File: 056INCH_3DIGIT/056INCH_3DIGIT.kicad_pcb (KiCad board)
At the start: 2 copper layers, 43.8 x 21 mm, 2 parts, among them U1 BA56-12SRWA

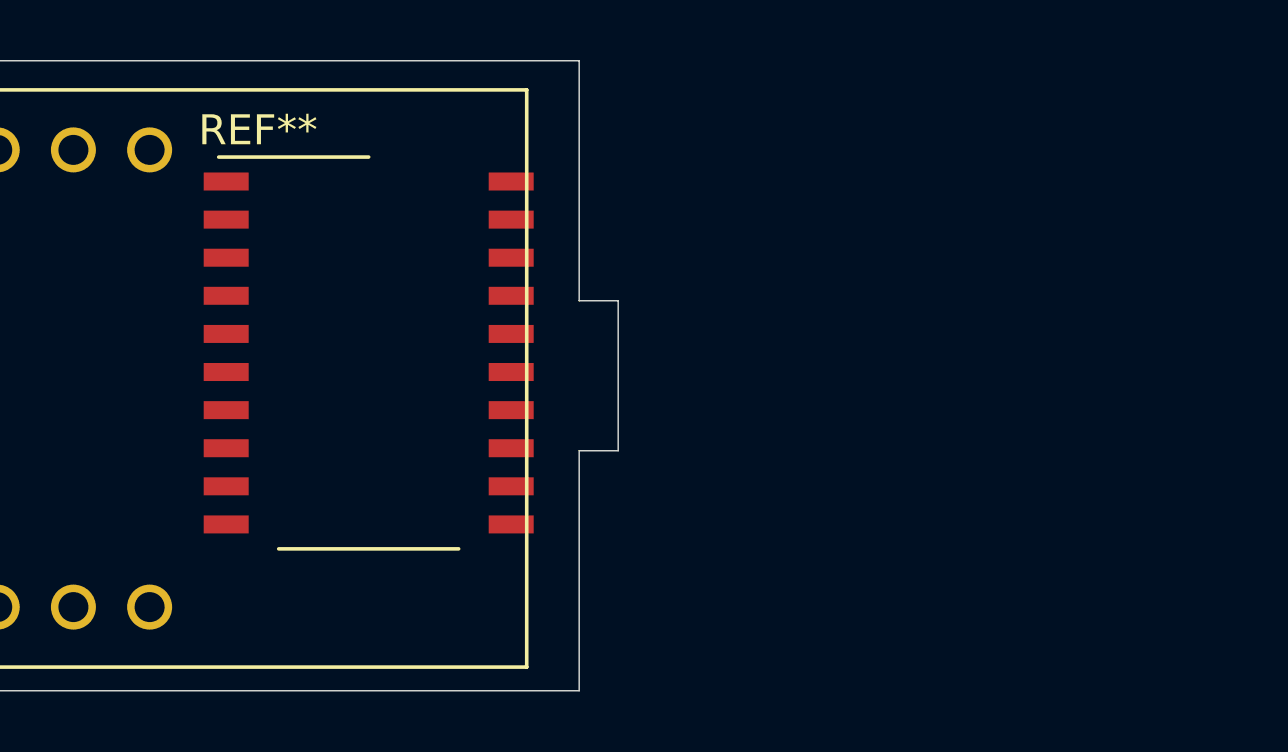
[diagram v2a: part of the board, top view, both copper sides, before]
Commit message: TM1637 symbol finished
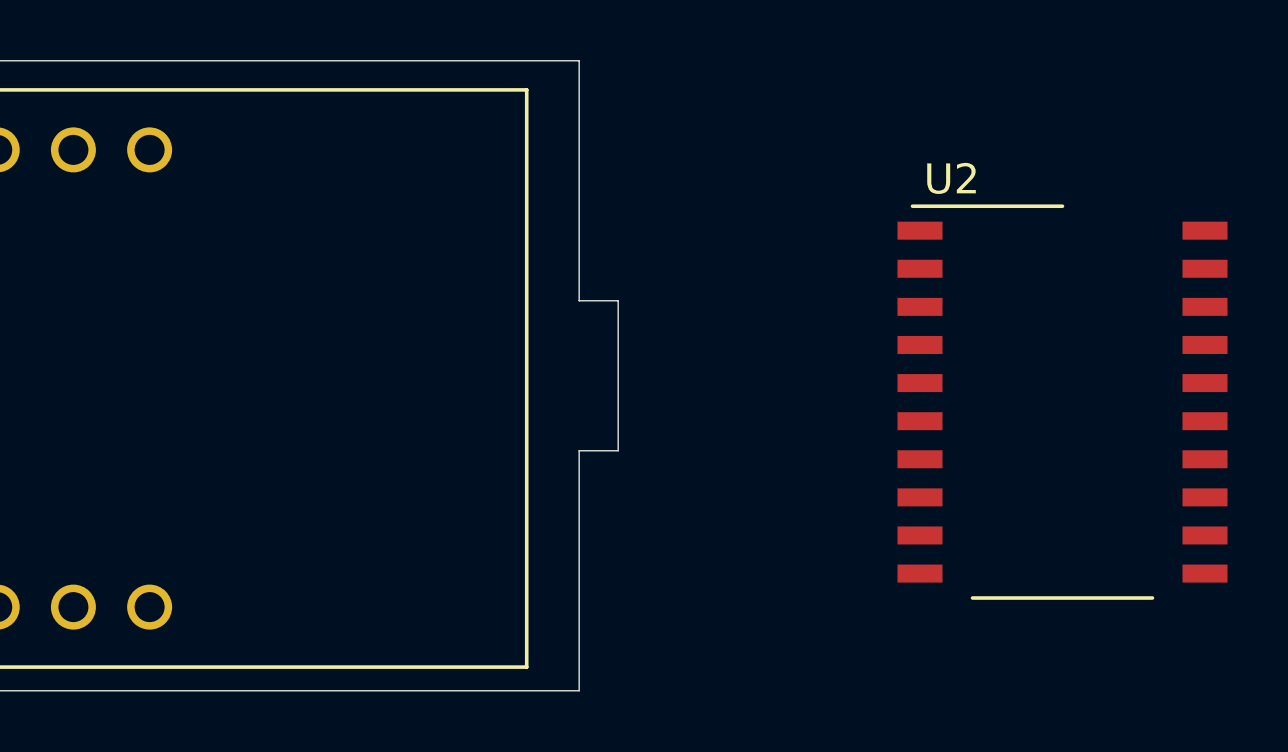
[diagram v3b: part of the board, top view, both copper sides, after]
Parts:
- removed REF**: SO-20_12.8x7.5mm_P1.27mm, Package_SO:SO-20_12.8x7.5mm_P1.27mm
- added U2: TM1637, Package_SO:SO-20_12.8x7.5mm_P1.27mm, F.Cu at (158.6, 111.4)
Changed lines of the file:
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@@
     (zones 0)
     (modules 2)
-    (nets 13)
+    (nets 30)
   )
   (page A4)
@@
   (net 11 "Net-(U1-Pad2)")
   (net 12 "Net-(U1-Pad1)")
+  (net 13 "Net-(U2-Pad18)")
+  (net 14 "Net-(U2-Pad17)")
+  (net 15 "Net-(U2-Pad16)")
+  (net 16 "Net-(U2-Pad15)")
+  (net 17 "Net-(U2-Pad14)")
+  (net 18 "Net-(U2-Pad13)")
+  (net 19 "Net-(U2-Pad12)")
+  (net 20 "Net-(U2-Pad11)")
+  (net 21 "Net-(U2-Pad10)")
+  (net 22 "Net-(U2-Pad8)")
+  (net 23 "Net-(U2-Pad7)")
+  (net 24 "Net-(U2-Pad1)")
+  (net 25 "Net-(U2-Pad2)")
+  (net 26 "Net-(U2-Pad3)")
+  (net 27 "Net-(U2-Pad4)")
+  (net 28 "Net-(U2-Pad5)")
+  (net 29 "Net-(U2-Pad6)")
   (net_class Default "This is the default net class."
     (clearance 0.2)
@@
     (add_net "Net-(U1-Pad8)")
     (add_net "Net-(U1-Pad9)")
+    (add_net "Net-(U2-Pad1)")
+    (add_net "Net-(U2-Pad10)")
+    (add_net "Net-(U2-Pad11)")
+    (add_net "Net-(U2-Pad12)")
+    (add_net "Net-(U2-Pad13)")
+    (add_net "Net-(U2-Pad14)")
+    (add_net "Net-(U2-Pad15)")
+    (add_net "Net-(U2-Pad16)")
+    (add_net "Net-(U2-Pad17)")
+    (add_net "Net-(U2-Pad18)")
+    (add_net "Net-(U2-Pad2)")
+    (add_net "Net-(U2-Pad3)")
+    (add_net "Net-(U2-Pad4)")
+    (add_net "Net-(U2-Pad5)")
+    (add_net "Net-(U2-Pad6)")
+    (add_net "Net-(U2-Pad7)")
+    (add_net "Net-(U2-Pad8)")
+  )
+  (module Package_SO:SO-20_12.8x7.5mm_P1.27mm (layer F.Cu)
+    (at 158.6103 111.379)
+    (descr "SO-20, 12.8x7.5mm, https://www.nxp.com/docs/en/data-sheet/SA605.pdf")
+    (tags "S0-20 ")
+    (attr smd)
+    (fp_text reference U2 (at -3.69 -7.42) (layer F.SilkS)
+      (effects (font (size 1 1) (thickness 0.15)))
+    )
+    (fp_text value TM1637 (at 0 7.99) (layer F.Fab)
+      (effects (font (size 1 1) (thickness 0.15)))
+    )
+    (fp_text user %R (at 0 0) (layer F.Fab)
+      (effects (font (size 1 1) (thickness 0.15)))
+    )
+    (fp_line (start -5.7 6.7) (end -5.7 -6.7) (layer F.CrtYd) (width 0.05))
+    (fp_line (start 5.7 6.7) (end -5.7 6.7) (layer F.CrtYd) (width 0.05))
+    (fp_line (start 5.7 -6.7) (end 5.7 6.7) (layer F.CrtYd) (width 0.05))
+    (fp_line (start -5.7 -6.7) (end 5.7 -6.7) (layer F.CrtYd) (width 0.05))
+    (fp_line (start -5 -6.53) (end 0 -6.53) (layer F.SilkS) (width 0.12))
+    (fp_line (start -3 6.53) (end 3 6.53) (layer F.SilkS) (width 0.12))
+    (fp_line (start -2.2 -5.4) (end -1.2 -6.4) (layer F.Fab) (width 0.1))
+    (fp_line (start -2.2 6.4) (end -2.2 -5.4) (layer F.Fab) (width 0.1))
+    (fp_line (start 2.2 6.4) (end -2.2 6.4) (layer F.Fab) (width 0.1))
+    (fp_line (start 2.2 -6.4) (end 2.2 6.4) (layer F.Fab) (width 0.1))
+    (fp_line (start -1.2 -6.4) (end 2.2 -6.4) (layer F.Fab) (width 0.1))
+    (pad 20 smd rect (at 4.75 -5.715) (size 1.5 0.6) (layers F.Cu F.Paste F.Mask))
+    (pad 19 smd rect (at 4.75 -4.445) (size 1.5 0.6) (layers F.Cu F.Paste F.Mask))
+    (pad 18 smd rect (at 4.75 -3.175) (size 1.5 0.6) (layers F.Cu F.Paste F.Mask)
+      (net 13 "Net-(U2-Pad18)"))
+    (pad 17 smd rect (at 4.75 -1.905) (size 1.5 0.6) (layers F.Cu F.Paste F.Mask)
+      (net 14 "Net-(U2-Pad17)"))
+    (pad 16 smd rect (at 4.75 -0.635) (size 1.5 0.6) (layers F.Cu F.Paste F.Mask)
+      (net 15 "Net-(U2-Pad16)"))
+    (pad 15 smd rect (at 4.75 0.635) (size 1.5 0.6) (layers F.Cu F.Paste F.Mask)
+      (net 16 "Net-(U2-Pad15)"))
+    (pad 14 smd rect (at 4.75 1.905) (size 1.5 0.6) (layers F.Cu F.Paste F.Mask)
+      (net 17 "Net-(U2-Pad14)"))
+    (pad 13 smd rect (at 4.75 3.175) (size 1.5 0.6) (layers F.Cu F.Paste F.Mask)
+      (net 18 "Net-(U2-Pad13)"))
+    (pad 12 smd rect (at 4.75 4.445) (size 1.5 0.6) (layers F.Cu F.Paste F.Mask)
+      (net 19 "Net-(U2-Pad12)"))
+    (pad 11 smd rect (at 4.75 5.715) (size 1.5 0.6) (layers F.Cu F.Paste F.Mask)
+      (net 20 "Net-(U2-Pad11)"))
+    (pad 10 smd rect (at -4.75 5.715) (size 1.5 0.6) (layers F.Cu F.Paste F.Mask)
+      (net 21 "Net-(U2-Pad10)"))
+    (pad 9 smd rect (at -4.75 4.445) (size 1.5 0.6) (layers F.Cu F.Paste F.Mask)
+      (net 21 "Net-(U2-Pad10)"))
+    (pad 8 smd rect (at -4.75 3.175) (size 1.5 0.6) (layers F.Cu F.Paste F.Mask)
+      (net 22 "Net-(U2-Pad8)"))
+    (pad 7 smd rect (at -4.75 1.905) (size 1.5 0.6) (layers F.Cu F.Paste F.Mask)
+      (net 23 "Net-(U2-Pad7)"))
+    (pad 1 smd rect (at -4.75 -5.715) (size 1.5 0.6) (layers F.Cu F.Paste F.Mask)
+      (net 24 "Net-(U2-Pad1)"))
+    (pad 2 smd rect (at -4.75 -4.445) (size 1.5 0.6) (layers F.Cu F.Paste F.Mask)
+      (net 25 "Net-(U2-Pad2)"))
+    (pad 3 smd rect (at -4.75 -3.175) (size 1.5 0.6) (layers F.Cu F.Paste F.Mask)
+      (net 26 "Net-(U2-Pad3)"))
+    (pad 4 smd rect (at -4.75 -1.905) (size 1.5 0.6) (layers F.Cu F.Paste F.Mask)
+      (net 27 "Net-(U2-Pad4)"))
+    (pad 5 smd rect (at -4.75 -0.635) (size 1.5 0.6) (layers F.Cu F.Paste F.Mask)
+      (net 28 "Net-(U2-Pad5)"))
+    (pad 6 smd rect (at -4.75 0.635) (size 1.5 0.6) (layers F.Cu F.Paste F.Mask)
+      (net 29 "Net-(U2-Pad6)"))
+    (model ${KISYS3DMOD}/Package_SO.3dshapes/SO-20_12.8x7.5mm_P1.27mm.wrl
+      (at (xyz 0 0 0))
+      (scale (xyz 1 1 1))
+      (rotate (xyz 0 0 0))
+    )
   )
   (module KINGBRIGHTUSA:BA56-12SRWA (layer F.Cu)
@@
       (at (xyz 0 0 0))
       (scale (xyz 1 1 1))
-      (rotate (xyz 0 0 0))
-    )
-  )
-  (module Package_SO:SO-20_12.8x7.5mm_P1.27mm (layer F.Cu)
-    (at 135.4836 109.7407)
-    (descr "SO-20, 12.8x7.5mm, https://www.nxp.com/docs/en/data-sheet/SA605.pdf")
-    (tags "S0-20 ")
-    (attr smd)
-    (fp_text reference REF** (at -3.69 -7.42) (layer F.SilkS)
-      (effects (font (size 1 1) (thickness 0.15)))
-    )
-    (fp_text value SO-20_12.8x7.5mm_P1.27mm (at 0 7.99) (layer F.Fab)
-      (effects (font (size 1 1) (thickness 0.15)))
-    )
-    (fp_text user %R (at 0 0) (layer F.Fab)
-      (effects (font (size 1 1) (thickness 0.15)))
-    )
-    (fp_line (start -5.7 6.7) (end -5.7 -6.7) (layer F.CrtYd) (width 0.05))
-    (fp_line (start 5.7 6.7) (end -5.7 6.7) (layer F.CrtYd) (width 0.05))
-    (fp_line (start 5.7 -6.7) (end 5.7 6.7) (layer F.CrtYd) (width 0.05))
-    (fp_line (start -5.7 -6.7) (end 5.7 -6.7) (layer F.CrtYd) (width 0.05))
-    (fp_line (start -5 -6.53) (end 0 -6.53) (layer F.SilkS) (width 0.12))
-    (fp_line (start -3 6.53) (end 3 6.53) (layer F.SilkS) (width 0.12))
-    (fp_line (start -2.2 -5.4) (end -1.2 -6.4) (layer F.Fab) (width 0.1))
-    (fp_line (start -2.2 6.4) (end -2.2 -5.4) (layer F.Fab) (width 0.1))
-    (fp_line (start 2.2 6.4) (end -2.2 6.4) (layer F.Fab) (width 0.1))
-    (fp_line (start 2.2 -6.4) (end 2.2 6.4) (layer F.Fab) (width 0.1))
-    (fp_line (start -1.2 -6.4) (end 2.2 -6.4) (layer F.Fab) (width 0.1))
-    (pad 20 smd rect (at 4.75 -5.715) (size 1.5 0.6) (layers F.Cu F.Paste F.Mask))
-    (pad 19 smd rect (at 4.75 -4.445) (size 1.5 0.6) (layers F.Cu F.Paste F.Mask))
-    (pad 18 smd rect (at 4.75 -3.175) (size 1.5 0.6) (layers F.Cu F.Paste F.Mask))
-    (pad 17 smd rect (at 4.75 -1.905) (size 1.5 0.6) (layers F.Cu F.Paste F.Mask))
-    (pad 16 smd rect (at 4.75 -0.635) (size 1.5 0.6) (layers F.Cu F.Paste F.Mask))
-    (pad 15 smd rect (at 4.75 0.635) (size 1.5 0.6) (layers F.Cu F.Paste F.Mask))
-    (pad 14 smd rect (at 4.75 1.905) (size 1.5 0.6) (layers F.Cu F.Paste F.Mask))
-    (pad 13 smd rect (at 4.75 3.175) (size 1.5 0.6) (layers F.Cu F.Paste F.Mask))
-    (pad 12 smd rect (at 4.75 4.445) (size 1.5 0.6) (layers F.Cu F.Paste F.Mask))
-    (pad 11 smd rect (at 4.75 5.715) (size 1.5 0.6) (layers F.Cu F.Paste F.Mask))
-    (pad 10 smd rect (at -4.75 5.715) (size 1.5 0.6) (layers F.Cu F.Paste F.Mask))
-    (pad 9 smd rect (at -4.75 4.445) (size 1.5 0.6) (layers F.Cu F.Paste F.Mask))
-    (pad 8 smd rect (at -4.75 3.175) (size 1.5 0.6) (layers F.Cu F.Paste F.Mask))
-    (pad 7 smd rect (at -4.75 1.905) (size 1.5 0.6) (layers F.Cu F.Paste F.Mask))
-    (pad 1 smd rect (at -4.75 -5.715) (size 1.5 0.6) (layers F.Cu F.Paste F.Mask))
-    (pad 2 smd rect (at -4.75 -4.445) (size 1.5 0.6) (layers F.Cu F.Paste F.Mask))
-    (pad 3 smd rect (at -4.75 -3.175) (size 1.5 0.6) (layers F.Cu F.Paste F.Mask))
-    (pad 4 smd rect (at -4.75 -1.905) (size 1.5 0.6) (layers F.Cu F.Paste F.Mask))
-    (pad 5 smd rect (at -4.75 -0.635) (size 1.5 0.6) (layers F.Cu F.Paste F.Mask))
-    (pad 6 smd rect (at -4.75 0.635) (size 1.5 0.6) (layers F.Cu F.Paste F.Mask))
-    (model ${KISYS3DMOD}/Package_SO.3dshapes/SO-20_12.8x7.5mm_P1.27mm.wrl
-      (at (xyz 0 0 0))
-      (scale (xyz 1 1 1))

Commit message: first connections schematic
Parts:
- moved U2 22.6 mm to (136.1, 110.4)
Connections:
- U2 pad 13: Net-(U2-Pad13) -> Net-(U1-Pad8)
- U2 pad 14: Net-(U2-Pad14) -> Net-(U1-Pad9)
- U2 pad 15: Net-(U2-Pad15) -> Net-(U1-Pad12)
- U2 pad 19: (no net) -> Net-(U2-Pad19)
- U2 pad 2: Net-(U2-Pad2) -> Net-(U1-Pad11)
- U2 pad 20: (no net) -> Net-(U2-Pad20)
- U2 pad 3: Net-(U2-Pad3) -> Net-(U1-Pad7)
- U2 pad 4: Net-(U2-Pad4) -> Net-(U1-Pad4)
- U2 pad 5: Net-(U2-Pad5) -> Net-(U1-Pad2)
- U2 pad 6: Net-(U2-Pad6) -> Net-(U1-Pad1)
- U2 pad 7: Net-(U2-Pad7) -> Net-(U1-Pad10)
- U2 pad 8: Net-(U2-Pad8) -> Net-(U1-Pad5)
- U2 pad 9: Net-(U2-Pad10) -> Net-(U1-Pad3)
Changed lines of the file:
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@@
     (zones 0)
     (modules 2)
-    (nets 30)
+    (nets 22)
   )
   (page A4)
@@
   (net 14 "Net-(U2-Pad17)")
   (net 15 "Net-(U2-Pad16)")
-  (net 16 "Net-(U2-Pad15)")
-  (net 17 "Net-(U2-Pad14)")
-  (net 18 "Net-(U2-Pad13)")
-  (net 19 "Net-(U2-Pad12)")
-  (net 20 "Net-(U2-Pad11)")
-  (net 21 "Net-(U2-Pad10)")
-  (net 22 "Net-(U2-Pad8)")
-  (net 23 "Net-(U2-Pad7)")
-  (net 24 "Net-(U2-Pad1)")
-  (net 25 "Net-(U2-Pad2)")
-  (net 26 "Net-(U2-Pad3)")
-  (net 27 "Net-(U2-Pad4)")
-  (net 28 "Net-(U2-Pad5)")
-  (net 29 "Net-(U2-Pad6)")
+  (net 16 "Net-(U2-Pad12)")
+  (net 17 "Net-(U2-Pad11)")
+  (net 18 "Net-(U2-Pad10)")
+  (net 19 "Net-(U2-Pad1)")
+  (net 20 "Net-(U2-Pad20)")
+  (net 21 "Net-(U2-Pad19)")
   (net_class Default "This is the default net class."
     (clearance 0.2)
@@
     (add_net "Net-(U2-Pad11)")
     (add_net "Net-(U2-Pad12)")
-    (add_net "Net-(U2-Pad13)")
-    (add_net "Net-(U2-Pad14)")
-    (add_net "Net-(U2-Pad15)")
     (add_net "Net-(U2-Pad16)")
     (add_net "Net-(U2-Pad17)")
     (add_net "Net-(U2-Pad18)")
-    (add_net "Net-(U2-Pad2)")
-    (add_net "Net-(U2-Pad3)")
-    (add_net "Net-(U2-Pad4)")
-    (add_net "Net-(U2-Pad5)")
-    (add_net "Net-(U2-Pad6)")
-    (add_net "Net-(U2-Pad7)")
-    (add_net "Net-(U2-Pad8)")
+    (add_net "Net-(U2-Pad19)")
+    (add_net "Net-(U2-Pad20)")
   )
   (module Package_SO:SO-20_12.8x7.5mm_P1.27mm (layer F.Cu)
-    (at 158.6103 111.379)
+    (at 136.0805 110.3503)
     (descr "SO-20, 12.8x7.5mm, https://www.nxp.com/docs/en/data-sheet/SA605.pdf")
     (tags "S0-20 ")
@@
     (fp_line (start 2.2 -6.4) (end 2.2 6.4) (layer F.Fab) (width 0.1))
     (fp_line (start -1.2 -6.4) (end 2.2 -6.4) (layer F.Fab) (width 0.1))
-    (pad 20 smd rect (at 4.75 -5.715) (size 1.5 0.6) (layers F.Cu F.Paste F.Mask))
-    (pad 19 smd rect (at 4.75 -4.445) (size 1.5 0.6) (layers F.Cu F.Paste F.Mask))
+    (pad 20 smd rect (at 4.75 -5.715) (size 1.5 0.6) (layers F.Cu F.Paste F.Mask)
+      (net 20 "Net-(U2-Pad20)"))
+    (pad 19 smd rect (at 4.75 -4.445) (size 1.5 0.6) (layers F.Cu F.Paste F.Mask)
+      (net 21 "Net-(U2-Pad19)"))
     (pad 18 smd rect (at 4.75 -3.175) (size 1.5 0.6) (layers F.Cu F.Paste F.Mask)
       (net 13 "Net-(U2-Pad18)"))
@@
       (net 15 "Net-(U2-Pad16)"))
     (pad 15 smd rect (at 4.75 0.635) (size 1.5 0.6) (layers F.Cu F.Paste F.Mask)
-      (net 16 "Net-(U2-Pad15)"))
+      (net 1 "Net-(U1-Pad12)"))
     (pad 14 smd rect (at 4.75 1.905) (size 1.5 0.6) (layers F.Cu F.Paste F.Mask)
-      (net 17 "Net-(U2-Pad14)"))
+      (net 4 "Net-(U1-Pad9)"))
     (pad 13 smd rect (at 4.75 3.175) (size 1.5 0.6) (layers F.Cu F.Paste F.Mask)
-      (net 18 "Net-(U2-Pad13)"))
+      (net 5 "Net-(U1-Pad8)"))
     (pad 12 smd rect (at 4.75 4.445) (size 1.5 0.6) (layers F.Cu F.Paste F.Mask)
-      (net 19 "Net-(U2-Pad12)"))
+      (net 16 "Net-(U2-Pad12)"))
     (pad 11 smd rect (at 4.75 5.715) (size 1.5 0.6) (layers F.Cu F.Paste F.Mask)
-      (net 20 "Net-(U2-Pad11)"))
+      (net 17 "Net-(U2-Pad11)"))
     (pad 10 smd rect (at -4.75 5.715) (size 1.5 0.6) (layers F.Cu F.Paste F.Mask)
-      (net 21 "Net-(U2-Pad10)"))
+      (net 18 "Net-(U2-Pad10)"))
     (pad 9 smd rect (at -4.75 4.445) (size 1.5 0.6) (layers F.Cu F.Paste F.Mask)
-      (net 21 "Net-(U2-Pad10)"))
+      (net 10 "Net-(U1-Pad3)"))
     (pad 8 smd rect (at -4.75 3.175) (size 1.5 0.6) (layers F.Cu F.Paste F.Mask)
-      (net 22 "Net-(U2-Pad8)"))
+      (net 8 "Net-(U1-Pad5)"))
     (pad 7 smd rect (at -4.75 1.905) (size 1.5 0.6) (layers F.Cu F.Paste F.Mask)
-      (net 23 "Net-(U2-Pad7)"))
+      (net 3 "Net-(U1-Pad10)"))
     (pad 1 smd rect (at -4.75 -5.715) (size 1.5 0.6) (layers F.Cu F.Paste F.Mask)
-      (net 24 "Net-(U2-Pad1)"))
+      (net 19 "Net-(U2-Pad1)"))
     (pad 2 smd rect (at -4.75 -4.445) (size 1.5 0.6) (layers F.Cu F.Paste F.Mask)
-      (net 25 "Net-(U2-Pad2)"))
+      (net 2 "Net-(U1-Pad11)"))
     (pad 3 smd rect (at -4.75 -3.175) (size 1.5 0.6) (layers F.Cu F.Paste F.Mask)
-      (net 26 "Net-(U2-Pad3)"))
+      (net 6 "Net-(U1-Pad7)"))
     (pad 4 smd rect (at -4.75 -1.905) (size 1.5 0.6) (layers F.Cu F.Paste F.Mask)
-      (net 27 "Net-(U2-Pad4)"))
+      (net 9 "Net-(U1-Pad4)"))
     (pad 5 smd rect (at -4.75 -0.635) (size 1.5 0.6) (layers F.Cu F.Paste F.Mask)
-      (net 28 "Net-(U2-Pad5)"))
+      (net 11 "Net-(U1-Pad2)"))
     (pad 6 smd rect (at -4.75 0.635) (size 1.5 0.6) (layers F.Cu F.Paste F.Mask)
-      (net 29 "Net-(U2-Pad6)"))
+      (net 12 "Net-(U1-Pad1)"))
     (model ${KISYS3DMOD}/Package_SO.3dshapes/SO-20_12.8x7.5mm_P1.27mm.wrl
       (at (xyz 0 0 0))
